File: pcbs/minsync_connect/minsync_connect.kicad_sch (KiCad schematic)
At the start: 2 parts, among them J1 Left, J2 Right

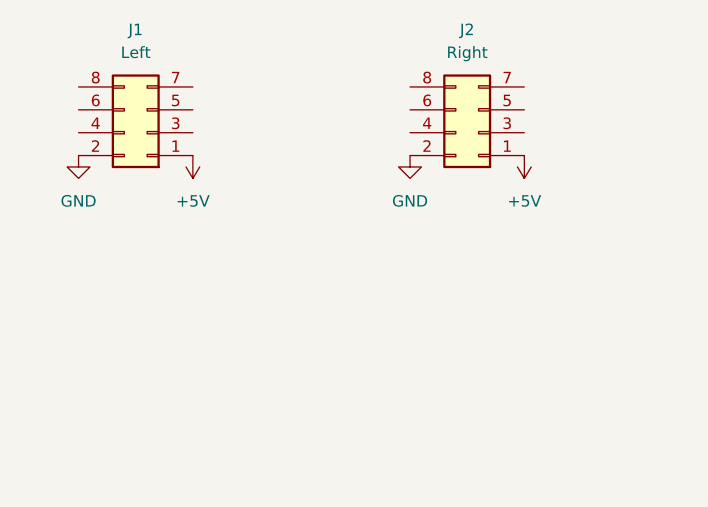
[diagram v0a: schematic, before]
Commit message: Implement minsync_connect v0.1
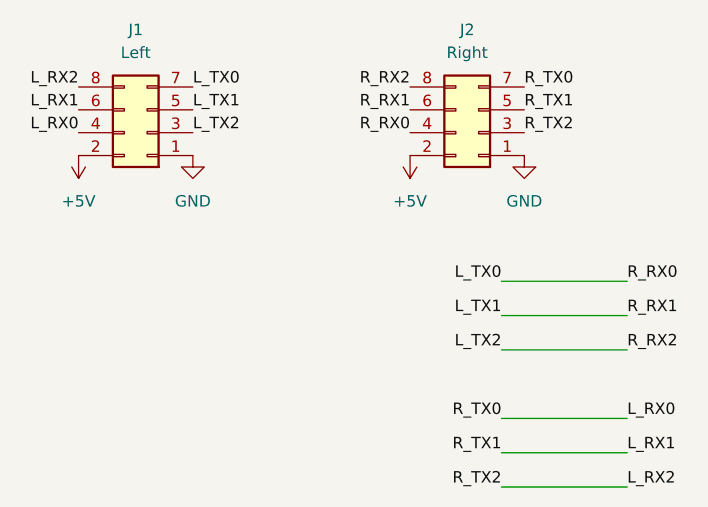
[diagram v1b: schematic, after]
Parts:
- J1, J2: footprint (none) -> RP2040_minimal_r2:pitopi_and_power
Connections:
- net +5V: now also J1.2 (Pin_2), J2.2 (Pin_2); no longer J1.1 (Pin_1), J2.1 (Pin_1)
- net GND: now also J1.1 (Pin_1), J2.1 (Pin_1); no longer J1.2 (Pin_2), J2.2 (Pin_2)
- net L_RX2: now reaches J2.3 (Pin_3)
- net L_RX2: now also J1.8 (Pin_8)
- net L_TX0: now reaches J2.4 (Pin_4)
- net L_TX0: now also J1.7 (Pin_7)
- net L_RX1: now reaches J2.5 (Pin_5)
- net L_RX1: now also J1.6 (Pin_6)
- net L_TX1: now reaches J2.6 (Pin_6)
- net L_TX1: now also J1.5 (Pin_5)
- net L_RX0: now reaches J2.7 (Pin_7)
- net L_RX0: now also J1.4 (Pin_4)
- net L_TX2: now reaches J2.8 (Pin_8)
- net L_TX2: now also J1.3 (Pin_3)
